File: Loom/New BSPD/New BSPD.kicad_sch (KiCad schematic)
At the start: 14 parts, among them J1 282087-1, J2 282087-1, J3 282105-1, K1 MCCMA51-S-DC12V-C, Q1 IRLZ44Z, U2 4081, U5 4011, U6 4081

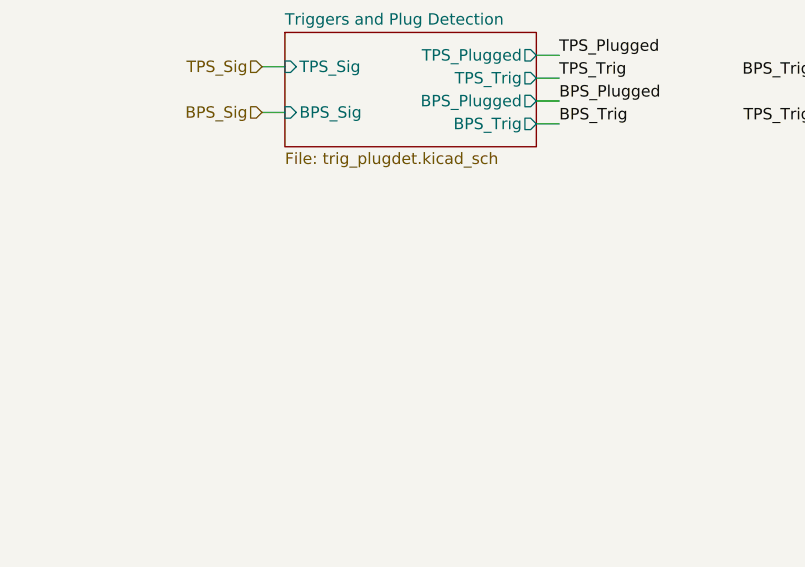
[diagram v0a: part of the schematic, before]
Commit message: Complete most of BSPD State Machine
TODO: Complete reset signal logic for state machine, to ensure
we don't power in into a metastable or invalid state.
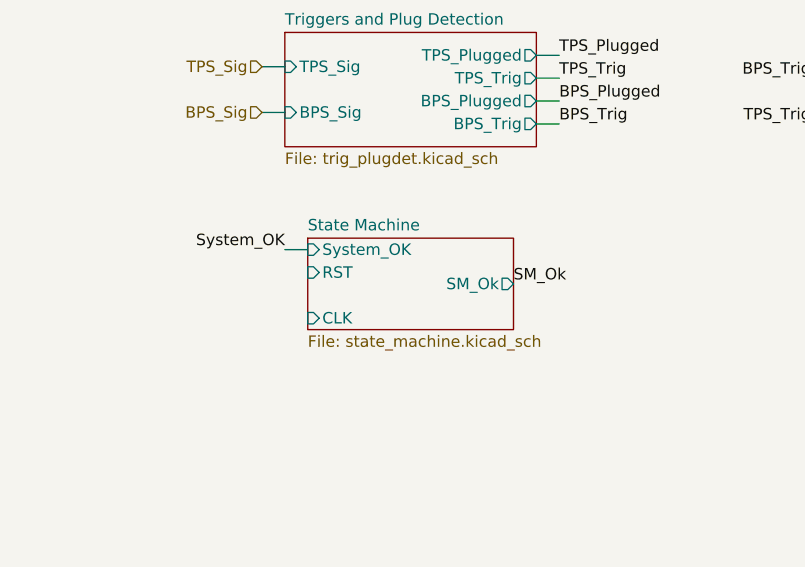
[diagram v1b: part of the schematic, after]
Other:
- added sheet State Machine (state_machine.kicad_sch)
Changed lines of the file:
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@@
+    (stroke (width 0) (type default))
+  )
+  (wire (pts (xy 49.53 76.2) (xy 52.07 76.2))
     (stroke (width 0) (type default))
   )
@@
     (effects (font (size 1.27 1.27)) (justify left bottom))
   )
+  (label "System_OK" (at 49.53 76.2 180) (fields_autoplaced)
+    (effects (font (size 1.27 1.27)) (justify right bottom))
+  )
   (label "TPS_Plugged" (at 80.01 54.61 0) (fields_autoplaced)
     (effects (font (size 1.27 1.27)) (justify left bottom))
@@
   (label "TPS_Trig" (at 107.95 62.23 180) (fields_autoplaced)
     (effects (font (size 1.27 1.27)) (justify right bottom))
+  )
+  (label "SM_Ok" (at 74.93 80.01 0) (fields_autoplaced)
+    (effects (font (size 1.27 1.27)) (justify left bottom))
   )
   (label "BPS_Plugged" (at 222.25 121.92 180) (fields_autoplaced)
@@
       )
     )
+  )
+  (sheet (at 52.07 74.93) (size 22.86 10.16) (fields_autoplaced)
+    (stroke (width 0.1524) (type solid))
+    (fill (color 0 0 0 0.0000))
+    (property "Sheetname" "State Machine" (at 52.07 74.2184 0)
+      (effects (font (size 1.27 1.27)) (justify left bottom))
+    )
+    (property "Sheetfile" "state_machine.kicad_sch" (at 52.07 85.6746 0)
+      (effects (font (size 1.27 1.27)) (justify left top))
+    )
+    (pin "CLK" input (at 52.07 83.82 180)
+      (effects (font (size 1.27 1.27)) (justify left))
+    )
+    (pin "System_OK" input (at 52.07 76.2 180)
+      (effects (font (size 1.27 1.27)) (justify left))
+    )
+    (pin "RST" input (at 52.07 78.74 180)
+      (effects (font (size 1.27 1.27)) (justify left))
+    )
+    (pin "SM_Ok" output (at 74.93 80.01 0)
+      (effects (font (size 1.27 1.27)) (justify right))
+    )
+    (instances
+      (project "New BSPD"
+        (path "/1f7c501a-057f-4634-92ce-528b01503799" (page "3"))
+      )
+    )

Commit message: Complete BSPD Schematic
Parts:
- removed U2, U6: 4081, symbol 4xxx:4081
- added U2: 4011, symbol 4xxx:4011
- added X1: ASZKDV-32.768KHz, Oscillator:Oscillator_SMD_Abracon_ASE-4Pin_3.2x2.5mm, symbol BSPD Symbols:ASZKDV-xxxMHz
- Q1: footprint Additional Footprints:TO-220-TabDown-NoHole -> Package_TO_SOT_THT:TO-220-3_Vertical
- U1: renamed from U5; footprint Package_DIP:DIP-14_W7.62mm_LongPads -> (none)
- renumbered D5 to D1, JP4 to JP1, JP3 to JP2, R4 to R2, R7 to R3
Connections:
- net +5V: now also X1.1 (EN), X1.4 (Vdd)
- net BPS_Plugged: now also U2.1
- net BPS_Trig: now also U1.8; no longer U1.1
- net GND: now also X1.2 (GND)
- net SD_Sig: now also U2.11
- net SM_Ok: now also U2.8
- net System_OK: now also U1.10; no longer U1.3
- net TPS_Plugged: now also U2.2
- net TPS_Trig: now also U1.9; no longer U1.2
- new net: U2.3, U2.5, U2.6
- new net: U2.4, U2.9
- new net: U2.10, U2.12, U2.13
- new net CLK: X1.3 (OUT)
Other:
- added sheet Power (power.kicad_sch)
- added sheet Reset Driver (reset.kicad_sch)

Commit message: Complete Schematic, Footprint Assignment, Start PCB Design
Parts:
- removed J1, J2: 282087-1, Additional Footprints:3 pin flying lead, symbol Connector:Conn_01x03_Female
- removed J3: 282105-1, Additional Footprints:3 pin flying lead, symbol Connector:Conn_01x03_Female
- added J1, J2, J3: Conn_01x03, BSPD_footprints:ATF13-3P-BM03, symbol Connector_Generic:Conn_01x03
- JP1, JP2: footprint (none) -> Jumper:SolderJumper-3_P1.3mm_Open_RoundedPad1.0x1.5mm
- Q1: footprint Package_TO_SOT_THT:TO-220-3_Vertical -> Package_TO_SOT_THT:TO-220-3_Horizontal_TabDown
- U1, U2: footprint (none) -> Package_DIP:DIP-14_W7.62mm_Socket
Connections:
- net BPS_Power: now also J1.3 (Pin_3)
- net BPS_Sig: now also J1.2 (Pin_2)
- net GND: now also J1.1 (Pin_1), J2.1 (Pin_1)
- net ShutdownC: now also J3.3 (Pin_3)
- net ShutdownNC: now also J3.2 (Pin_2)
- net ShutdownNO: now also J3.1 (Pin_1)
- net TPS_Power: now also J2.3 (Pin_3)
- net TPS_Sig: now also J2.2 (Pin_2)
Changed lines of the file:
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@@
     (stroke (width 0) (type default))
   )
-  (text "NO\nNC\nC\n" (at 261.62 76.2 0)
+  (text "NO\nNC\nC\n" (at 262.89 76.2 0)
     (effects (font (size 1.5 1.5)) (justify left bottom))
   )
@@
       (effects (font (size 1.27 1.27)))
     )
-    (property "Footprint" "" (at 209.55 132.08 0)
+    (property "Footprint" "Package_DIP:DIP-14_W7.62mm_Socket" (at 209.55 132.08 0)
       (effects (font (size 1.27 1.27)) hide)
     )
@@
       (effects (font (size 1.27 1.27)))
     )
-    (property "Footprint" "" (at 115.57 59.69 0)
+    (property "Footprint" "Package_DIP:DIP-14_W7.62mm_Socket" (at 115.57 59.69 0)
       (effects (font (size 1.27 1.27)) hide)
     )
@@
       (effects (font (size 1.27 1.27)))
     )
-    (property "Footprint" "" (at 226.06 132.08 0)
+    (property "Footprint" "Package_DIP:DIP-14_W7.62mm_Socket" (at 226.06 132.08 0)
       (effects (font (size 1.27 1.27)) hide)
     )
@@
     )
   )
-  (symbol (lib_id "Connector:Conn_01x03_Female") (at 261.62 72.39 0) (unit 1)
-    (in_bom yes) (on_board yes) (dnp no)
-    (property "Reference" "J3" (at 260.985 62.23 0)
-      (effects (font (size 1.27 1.27)))
-    )
-    (property "Value" "282105-1" (at 261.62 64.77 0)
-      (effects (font (size 1.27 1.27)))
-    )
-    (property "Footprint" "Additional Footprints:3 pin flying lead" (at 261.62 72.39 0)
-      (effects (font (size 1.27 1.27)) hide)
-    )
-    (property "Datasheet" "https://www.te.com/usa-en/product-282105-1.datasheet.pdf" (at 261.62 72.39 0)
-      (effects (font (size 1.27 1.27)) hide)
-    )
-    (pin "1")
-    (pin "2")
-    (pin "3")
-    (instances
-      (project "New BSPD"
-        (path "/1f7c501a-057f-4634-92ce-528b01503799"
-          (reference "J3") (unit 1)
-        )
-      )
-      (project "BSPD - FSG"
-        (path "/ea40ab7b-80c4-4cf6-acf9-83a05b0cd5a6"
-          (reference "J?") (unit 1)
-        )
-      )
-    )
-  )
   (symbol (lib_id "power:+12V") (at 43.18 25.4 0) (unit 1)
     (in_bom yes) (on_board yes) (dnp no) (fields_autoplaced)
@@
       (effects (font (size 1.27 1.27)) hide)
     )
-    (property "Footprint" "" (at 38.1 26.67 0)
+    (property "Footprint" "Jumper:SolderJumper-3_P1.3mm_Open_RoundedPad1.0x1.5mm" (at 38.1 26.67 0)
       (effects (font (size 1.27 1.27)) hide)
     )
@@
     )
   )
+  (symbol (lib_id "Connector_Generic:Conn_01x03") (at 31.75 38.1 180) (unit 1)
+    (in_bom yes) (on_board yes) (dnp no) (fields_autoplaced)
+    (property "Reference" "J1" (at 31.75 29.21 0)
+      (effects (font (size 1.27 1.27)))
+    )
+    (property "Value" "Conn_01x03" (at 31.75 31.75 0)
+      (effects (font (size 1.27 1.27)))
+    )
+    (property "Footprint" "BSPD_footprints:ATF13-3P-BM03" (at 31.75 38.1 0)
+      (effects (font (size 1.27 1.27)) hide)
+    )
+    (property "Datasheet" "~" (at 31.75 38.1 0)
+      (effects (font (size 1.27 1.27)) hide)
+    )
+    (pin "1")
+    (pin "2")
+    (pin "3")
+    (instances
+      (project "New BSPD"
+        (path "/1f7c501a-057f-4634-92ce-528b01503799"
+          (reference "J1") (unit 1)
+        )
+      )
+    )
+  )
   (symbol (lib_id "power:+5V") (at 82.55 25.4 0) (unit 1)
     (in_bom yes) (on_board yes) (dnp no) (fields_autoplaced)
@@
         (path "/ea40ab7b-80c4-4cf6-acf9-83a05b0cd5a6"
           (reference "#PWR?") (unit 1)
+        )
+      )
+    )
+  )
+  (symbol (lib_id "Connector_Generic:Conn_01x03") (at 81.28 38.1 180) (unit 1)
+    (in_bom yes) (on_board yes) (dnp no) (fields_autoplaced)
+    (property "Reference" "J2" (at 81.28 29.21 0)
+      (effects (font (size 1.27 1.27)))
+    )
+    (property "Value" "Conn_01x03" (at 81.28 31.75 0)
+      (effects (font (size 1.27 1.27)))
+    )
+    (property "Footprint" "BSPD_footprints:ATF13-3P-BM03" (at 81.28 38.1 0)
+      (effects (font (size 1.27 1.27)) hide)
+    )
+    (property "Datasheet" "~" (at 81.28 38.1 0)
+      (effects (font (size 1.27 1.27)) hide)
+    )
+    (pin "1")
+    (pin "2")
+    (pin "3")
+    (instances
+      (project "New BSPD"
+        (path "/1f7c501a-057f-4634-92ce-528b01503799"
+          (reference "J2") (unit 1)
         )
       )
@@
       (effects (font (size 1.27 1.27)))
     )
-    (property "Footprint" "" (at 260.35 125.73 0)
+    (property "Footprint" "Package_DIP:DIP-14_W7.62mm_Socket" (at 260.35 125.73 0)
       (effects (font (size 1.27 1.27)) hide)
     )
@@
       (effects (font (size 1.27 1.27)))
     )
-    (property "Footprint" "" (at 243.84 125.73 0)
+    (property "Footprint" "Package_DIP:DIP-14_W7.62mm_Socket" (at 243.84 125.73 0)
       (effects (font (size 1.27 1.27)) hide)
     )
@@
     )
   )
+  (symbol (lib_id "Connector_Generic:Conn_01x03") (at 261.62 72.39 0) (unit 1)
+    (in_bom yes) (on_board yes) (dnp no)
+    (property "Reference" "J3" (at 260.35 67.31 0)
+      (effects (font (size 1.27 1.27)) (justify left))
+    )
+    (property "Value" "Conn_01x03" (at 260.35 64.77 0)
+      (effects (font (size 1.27 1.27)) (justify left))
+    )
+    (property "Footprint" "BSPD_footprints:ATF13-3P-BM03" (at 261.62 72.39 0)
+      (effects (font (size 1.27 1.27)) hide)
+    )
+    (property "Datasheet" "~" (at 261.62 72.39 0)
+      (effects (font (size 1.27 1.27)) hide)
+    )
+    (pin "1")
+    (pin "2")
+    (pin "3")
+    (instances
+      (project "New BSPD"
+        (path "/1f7c501a-057f-4634-92ce-528b01503799"
+          (reference "J3") (unit 1)
+        )
+      )
+    )
+  )
   (symbol (lib_id "power:GND") (at 227.33 95.25 0) (unit 1)
     (in_bom yes) (on_board yes) (dnp no) (fields_autoplaced)
@@
       (effects (font (size 1.27 1.27)) hide)
     )
-    (property "Footprint" "" (at 87.63 26.67 0)
+    (property "Footprint" "Jumper:SolderJumper-3_P1.3mm_Open_RoundedPad1.0x1.5mm" (at 87.63 26.67 0)
       (effects (font (size 1.27 1.27)) hide)
     )
@@
       (effects (font (size 1.27 1.27)) (justify left))
     )
-    (property "Footprint" "Package_TO_SOT_THT:TO-220-3_Vertical" (at 231.14 92.075 0)
+    (property "Footprint" "Package_TO_SOT_THT:TO-220-3_Horizontal_TabDown" (at 231.14 92.075 0)
       (effects (font (size 1.27 1.27) italic) (justify left) hide)
     )
@@
         (path "/ea40ab7b-80c4-4cf6-acf9-83a05b0cd5a6"
           (reference "Q?") (unit 1)
-        )
-      )
-    )
-  )
-  (symbol (lib_id "Connector:Conn_01x03_Female") (at 31.75 38.1 180) (unit 1)
-    (in_bom yes) (on_board yes) (dnp no)
-    (property "Reference" "J1" (at 27.94 31.75 0)
-      (effects (font (size 1.27 1.27)))
-    )
-    (property "Value" "282087-1" (at 25.4 35.56 0)
-      (effects (font (size 1.27 1.27)))
-    )
-    (property "Footprint" "Additional Footprints:3 pin flying lead" (at 31.75 38.1 0)
-      (effects (font (size 1.27 1.27)) hide)
-    )
-    (property "Datasheet" "https://www.te.com/usa-en/product-282087-1.html" (at 31.75 38.1 0)
-      (effects (font (size 1.27 1.27)) hide)
-    )
-    (pin "1")
-    (pin "2")
-    (pin "3")
-    (instances
-      (project "New BSPD"
-        (path "/1f7c501a-057f-4634-92ce-528b01503799"
-          (reference "J1") (unit 1)
-        )
-      )
-      (project "BSPD - FSG"
-        (path "/ea40ab7b-80c4-4cf6-acf9-83a05b0cd5a6"
-          (reference "J?") (unit 1)
         )
       )
@@
         )
       )
-    )
-  )
-  (symbol (lib_id "Connector:Conn_01x03_Female") (at 81.28 38.1 180) (unit 1)
-    (in_bom yes) (on_board yes) (dnp no)
-    (property "Reference" "J2" (at 77.47 31.75 0)
-      (effects (font (size 1.27 1.27)))
-    )
-    (property "Value" "282087-1" (at 74.93 35.56 0)
-      (effects (font (size 1.27 1.27)))
-    )
-    (property "Footprint" "Additional Footprints:3 pin flying lead" (at 81.28 38.1 0)
-      (effects (font (size 1.27 1.27)) hide)
-    )
-    (property "Datasheet" "https://www.te.com/usa-en/product-282087-1.html" (at 81.28 38.1 0)
-      (effects (font (size 1.27 1.27)) hide)
-    )
-    (pin "1")
-    (pin "2")
-    (pin "3")
-    (instances
-      (project "New BSPD"
-        (path "/1f7c501a-057f-4634-92ce-528b01503799"
-          (reference "J2") (unit 1)
-        )
-      )
-      (project "BSPD - FSG"
-        (path "/ea40ab7b-80c4-4cf6-acf9-83a05b0cd5a6"
-          (reference "J?") (unit 1)
-        )
-      )

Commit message: Add State, Shutdown LEDs, Complete rough board layout
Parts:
- added D8: LED, LED_THT:LED_D5.0mm, symbol Device:LED
- added R11: 220R, Resistor_THT:R_Axial_DIN0207_L6.3mm_D2.5mm_P7.62mm_Horizontal, symbol Device:R
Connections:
- net GND: now also D8.1 (K)
- net SD_Sig: now also R11.2
- new net: D8.2 (A), R11.1
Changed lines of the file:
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@@
     (effects (font (size 1.27 1.27)) (justify right bottom))
+  )
+  (label "SD_Sig" (at 248.92 139.7 0) (fields_autoplaced)
+    (effects (font (size 1.27 1.27)) (justify left bottom))
   )
   (label "SM_Ok" (at 77.47 80.01 0) (fields_autoplaced)
@@
     )
   )
+  (symbol (lib_id "Device:R") (at 248.92 143.51 180) (unit 1)
+    (in_bom yes) (on_board yes) (dnp no) (fields_autoplaced)
+    (property "Reference" "R11" (at 250.698 142.6753 0)
+      (effects (font (size 1.27 1.27)) (justify right))
+    )
+    (property "Value" "220R" (at 250.698 145.2122 0)
+      (effects (font (size 1.27 1.27)) (justify right))
+    )
+    (property "Footprint" "Resistor_THT:R_Axial_DIN0207_L6.3mm_D2.5mm_P7.62mm_Horizontal" (at 250.698 143.51 90)
+      (effects (font (size 1.27 1.27)) hide)
+    )
+    (property "Datasheet" "~" (at 248.92 143.51 0)
+      (effects (font (size 1.27 1.27)) hide)
+    )
+    (pin "1")
+    (pin "2")
+    (instances
+      (project "New BSPD"
+        (path "/1f7c501a-057f-4634-92ce-528b01503799"
+          (reference "R11") (unit 1)
+        )
+        (path "/1f7c501a-057f-4634-92ce-528b01503799/81a2d232-b56a-457d-8f4d-f7bde46d944b"
+          (reference "R7") (unit 1)
+        )
+        (path "/1f7c501a-057f-4634-92ce-528b01503799/c1af1d02-f1c8-42b8-8d3c-ac3883e05aae"
+          (reference "R10") (unit 1)
+        )
+      )
+      (project "BSPD - FSG"
+        (path "/ea40ab7b-80c4-4cf6-acf9-83a05b0cd5a6"
+          (reference "R?") (unit 1)
+        )
+      )
+    )
+  )
   (symbol (lib_id "BSPD Symbols:ASZKDV-xxxMHz") (at 156.21 36.83 0) (unit 1)
     (in_bom yes) (on_board yes) (dnp no)
@@
     )
   )
+  (symbol (lib_id "power:GND") (at 248.92 154.94 0) (unit 1)
+    (in_bom yes) (on_board yes) (dnp no) (fields_autoplaced)
+    (property "Reference" "#PWR046" (at 248.92 161.29 0)
+      (effects (font (size 1.27 1.27)) hide)
+    )
+    (property "Value" "GND" (at 248.92 159.3834 0)
+      (effects (font (size 1.27 1.27)))
+    )
+    (property "Footprint" "" (at 248.92 154.94 0)
+      (effects (font (size 1.27 1.27)) hide)
+    )
+    (property "Datasheet" "" (at 248.92 154.94 0)
+      (effects (font (size 1.27 1.27)) hide)
+    )
+    (pin "1")
+    (instances
+      (project "New BSPD"
+        (path "/1f7c501a-057f-4634-92ce-528b01503799"
+          (reference "#PWR046") (unit 1)
+        )
+        (path "/1f7c501a-057f-4634-92ce-528b01503799/81a2d232-b56a-457d-8f4d-f7bde46d944b"
+          (reference "#PWR022") (unit 1)
+        )
+        (path "/1f7c501a-057f-4634-92ce-528b01503799/c1af1d02-f1c8-42b8-8d3c-ac3883e05aae"
+          (reference "#PWR045") (unit 1)
+        )
+      )
+      (project "BSPD - FSG"
+        (path "/ea40ab7b-80c4-4cf6-acf9-83a05b0cd5a6"
+          (reference "#PWR?") (unit 1)
+        )
+      )
+    )
+  )
   (symbol (lib_id "power:+5V") (at 53.34 29.21 0) (unit 1)
     (in_bom yes) (on_board yes) (dnp no)
@@
         )
       )
+    )
+  )
+  (symbol (lib_id "Device:LED") (at 248.92 151.13 90) (unit 1)
+    (in_bom yes) (on_board yes) (dnp no) (fields_autoplaced)
+    (property "Reference" "D8" (at 251.841 151.8828 90)
+      (effects (font (size 1.27 1.27)) (justify right))
+    )
+    (property "Value" "LED" (at 251.841 154.4197 90)
+      (effects (font (size 1.27 1.27)) (justify right))
+    )
+    (property "Footprint" "LED_THT:LED_D5.0mm" (at 248.92 151.13 0)
+      (effects (font (size 1.27 1.27)) hide)
+    )
+    (property "Datasheet" "~" (at 248.92 151.13 0)
+      (effects (font (size 1.27 1.27)) hide)
+    )
+    (pin "1")
+    (pin "2")
+    (instances
+      (project "New BSPD"
+        (path "/1f7c501a-057f-4634-92ce-528b01503799"
+          (reference "D8") (unit 1)
+        )
+        (path "/1f7c501a-057f-4634-92ce-528b01503799/81a2d232-b56a-457d-8f4d-f7bde46d944b"
+          (reference "D5") (unit 1)
+        )
+        (path "/1f7c501a-057f-4634-92ce-528b01503799/c1af1d02-f1c8-42b8-8d3c-ac3883e05aae"
+          (reference "D7") (unit 1)
+        )
+      )
+      (project "BSPD - FSG"
+        (path "/ea40ab7b-80c4-4cf6-acf9-83a05b0cd5a6"
+          (reference "D?") (unit 1)
+        )
+      )

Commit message: Add filtering capacitor for crystal power
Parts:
- added C2: 10u, Capacitor_SMD:C_0603_1608Metric_Pad1.08x0.95mm_HandSolder, symbol Device:C
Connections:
- net +5V: now also C2.1
- net GND: now also C2.2
